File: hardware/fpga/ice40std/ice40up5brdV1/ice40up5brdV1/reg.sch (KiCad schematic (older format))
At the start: 11 parts

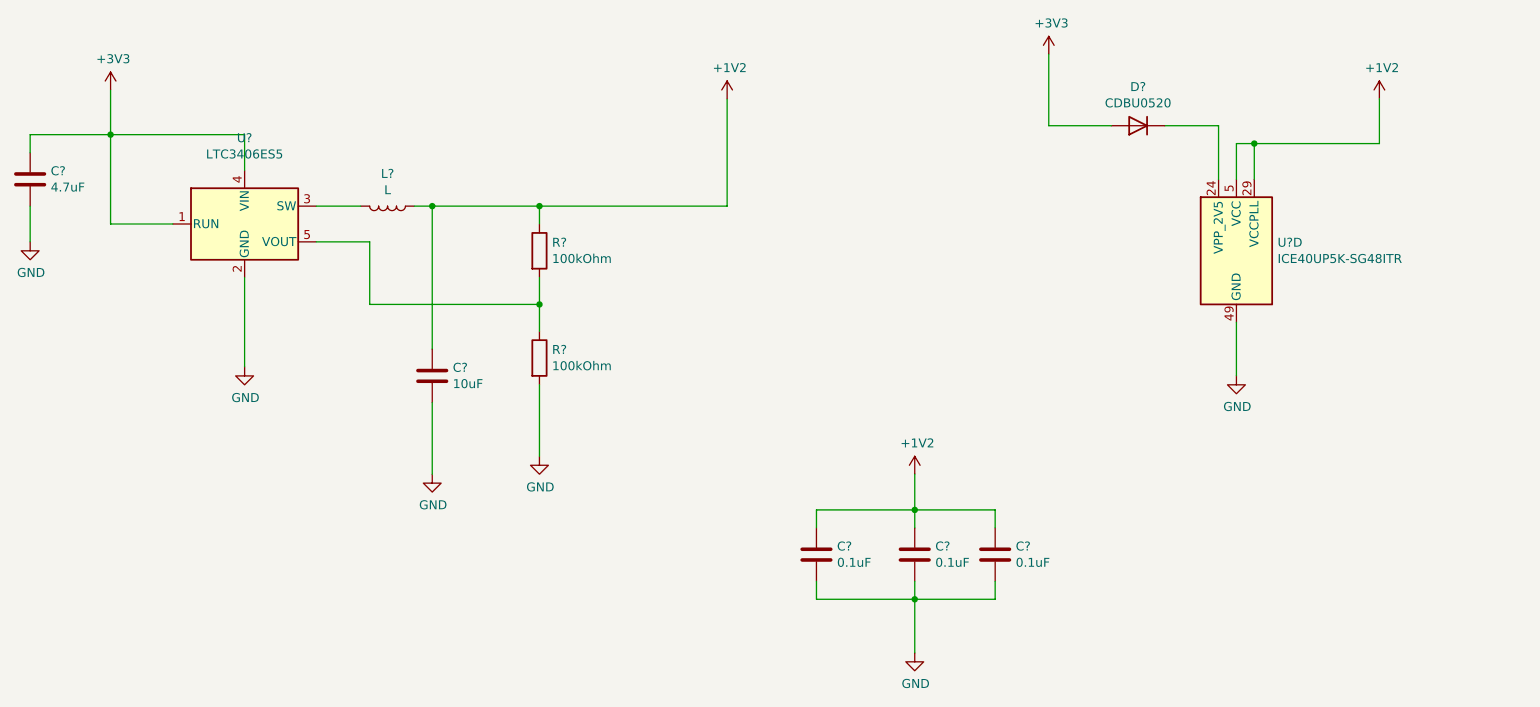
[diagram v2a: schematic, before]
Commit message: usb => mcu => ice40 fpga => NAND flash bridge started
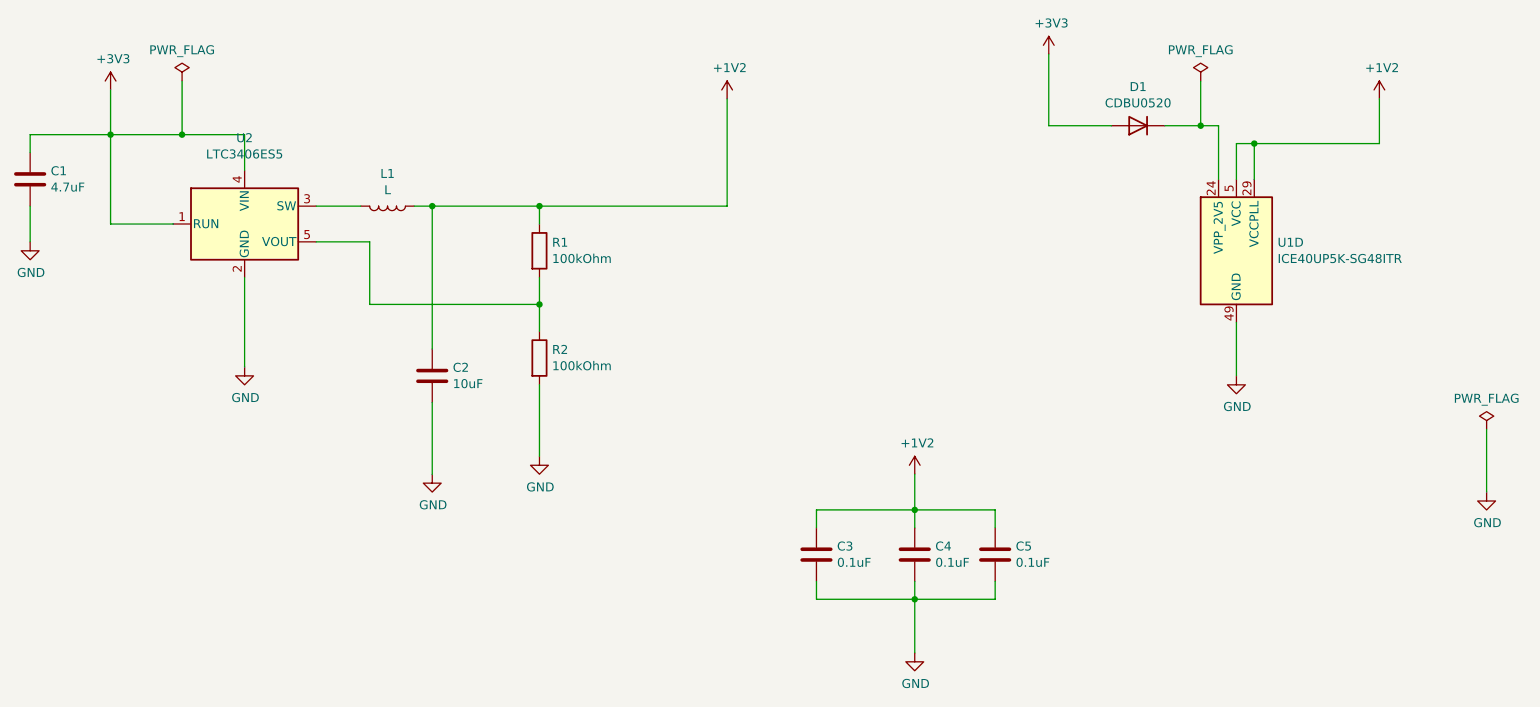
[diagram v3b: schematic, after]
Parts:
- gave numbers to parts that had none: 11
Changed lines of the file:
@@
 $EndDescr
 $Comp
-L FPGA_Lattice:ICE40UP5K-SG48ITR U?
+L FPGA_Lattice:ICE40UP5K-SG48ITR U1
 U 4 1 60A7161F
 P 7850 3250
-F 0 "U?" H 8080 3296 50  0000 L CNN
+F 0 "U1" H 8080 3296 50  0000 L CNN
 F 1 "ICE40UP5K-SG48ITR" H 8080 3205 50  0000 L CNN
 F 2 "Package_DFN_QFN:QFN-48-1EP_7x7mm_P0.5mm_EP5.6x5.6mm" H 7850 1900 50  0001 C CNN
@@
 $EndComp
 $Comp
-L Regulator_Switching:LTC3406ES5 U?
+L Regulator_Switching:LTC3406ES5 U2
 U 1 1 60A7BA3D
 P 2300 3100
-F 0 "U?" H 2300 3581 50  0000 C CNN
+F 0 "U2" H 2300 3581 50  0000 C CNN
 F 1 "LTC3406ES5" H 2300 3490 50  0000 C CNN
 F 2 "Package_TO_SOT_SMD:TSOT-23-5" H 3000 2850 50  0001 C CNN
@@
 $EndComp
 $Comp
-L Device:D D?
+L Device:D D1
 U 1 1 60A801A2
 P 7300 2550
-F 0 "D?" H 7300 2333 50  0000 C CNN
+F 0 "D1" H 7300 2333 50  0000 C CNN
 F 1 "CDBU0520" H 7300 2424 50  0000 C CNN
 F 2 "Diode_SMD:D_0603_1608Metric" H 7300 2550 50  0001 C CNN
@@
 $EndComp
 $Comp
-L Device:L L?
+L Device:L L1
 U 1 1 60A846BB
 P 3100 3000
-F 0 "L?" V 2919 3000 50  0000 C CNN
+F 0 "L1" V 2919 3000 50  0000 C CNN
 F 1 "L" V 3010 3000 50  0000 C CNN
 F 2 "Inductor_SMD:L_1210_3225Metric" H 3100 3000 50  0001 C CNN
@@
 $EndComp
 $Comp
-L Device:R R?
+L Device:R R1
 U 1 1 60A869B1
 P 3950 3250
-F 0 "R?" H 4020 3296 50  0000 L CNN
+F 0 "R1" H 4020 3296 50  0000 L CNN
 F 1 "100kOhm" H 4020 3205 50  0000 L CNN
 F 2 "Resistor_SMD:R_0402_1005Metric" V 3880 3250 50  0001 C CNN
@@
 $EndComp
 $Comp
-L Device:R R?
+L Device:R R2
 U 1 1 60A86DB5
 P 3950 3850
-F 0 "R?" H 4020 3896 50  0000 L CNN
+F 0 "R2" H 4020 3896 50  0000 L CNN
 F 1 "100kOhm" H 4020 3805 50  0000 L CNN
 F 2 "Resistor_SMD:R_0402_1005Metric" V 3880 3850 50  0001 C CNN
@@
 $EndComp
 $Comp
-L power:GND #PWR?
+L power:GND #PWR05
 U 1 1 60A872CB
 P 3950 4400
-F 0 "#PWR?" H 3950 4150 50  0001 C CNN
+F 0 "#PWR05" H 3950 4150 50  0001 C CNN
 F 1 "GND" H 3955 4227 50  0000 C CNN
 F 2 "" H 3950 4400 50  0001 C CNN
@@
 	3950 3550 3950 3400
 $Comp
-L power:GND #PWR?
+L power:GND #PWR03
 U 1 1 60A8868D
 P 2300 3900
-F 0 "#PWR?" H 2300 3650 50  0001 C CNN
+F 0 "#PWR03" H 2300 3650 50  0001 C CNN
 F 1 "GND" H 2305 3727 50  0000 C CNN
 F 2 "" H 2300 3900 50  0001 C CNN
@@
 	2300 3400 2300 3900
 $Comp
-L power:+3V3 #PWR?
+L power:+3V3 #PWR02
 U 1 1 60A899B6
 P 1550 2350
-F 0 "#PWR?" H 1550 2200 50  0001 C CNN
+F 0 "#PWR02" H 1550 2200 50  0001 C CNN
 F 1 "+3V3" H 1565 2523 50  0000 C CNN
 F 2 "" H 1550 2350 50  0001 C CNN
@@
 	2300 2800 2300 2600
 Wire Wire Line
-	2300 2600 1550 2600
+	2300 2600 1950 2600
 Connection ~ 1550 2600
 Wire Wire Line
 	1550 2600 1550 3100
 $Comp
-L Device:C C?
+L Device:C C1
 U 1 1 60A8A29C
 P 1100 2850
-F 0 "C?" H 1215 2896 50  0000 L CNN
+F 0 "C1" H 1215 2896 50  0000 L CNN
 F 1 "4.7uF" H 1215 2805 50  0000 L CNN
 F 2 "Capacitor_SMD:C_0402_1005Metric" H 1138 2700 50  0001 C CNN
@@
 	1100 2600 1550 2600
 $Comp
-L power:GND #PWR?
+L power:GND #PWR01
 U 1 1 60A8AD40
 P 1100 3200
-F 0 "#PWR?" H 1100 2950 50  0001 C CNN
+F 0 "#PWR01" H 1100 2950 50  0001 C CNN
 F 1 "GND" H 1105 3027 50  0000 C CNN
 F 2 "" H 1100 3200 50  0001 C CNN
@@
 	1100 3000 1100 3200
 $Comp
-L Device:C C?
+L Device:C C2
 U 1 1 60A8B955
 P 3350 3950
-F 0 "C?" H 3465 3996 50  0000 L CNN
+F 0 "C2" H 3465 3996 50  0000 L CNN
 F 1 "10uF" H 3465 3905 50  0000 L CNN
 F 2 "Capacitor_SMD:C_0603_1608Metric" H 3388 3800 50  0001 C CNN
@@
 	3350 3000 3950 3000
 $Comp
-L power:GND #PWR?
+L power:GND #PWR04
 U 1 1 60A8CBDB
 P 3350 4500
-F 0 "#PWR?" H 3350 4250 50  0001 C CNN
+F 0 "#PWR04" H 3350 4250 50  0001 C CNN
 F 1 "GND" H 3355 4327 50  0000 C CNN
 F 2 "" H 3350 4500 50  0001 C CNN
@@
 	3350 4100 3350 4500
 $Comp
-L power:+1V2 #PWR?
+L power:+1V2 #PWR06
 U 1 1 60A8DB44
 P 5000 2400
-F 0 "#PWR?" H 5000 2250 50  0001 C CNN
+F 0 "#PWR06" H 5000 2250 50  0001 C CNN
 F 1 "+1V2" H 5015 2573 50  0000 C CNN
 F 2 "" H 5000 2400 50  0001 C CNN
@@
 Connection ~ 3950 3000
 Wire Wire Line
-	7450 2550 7750 2550
+	7450 2550 7650 2550
 Wire Wire Line
 	7750 2550 7750 2850
 $Comp
-L power:+3V3 #PWR?
+L power:+3V3 #PWR09
 U 1 1 60A9198E
 P 6800 2150
-F 0 "#PWR?" H 6800 2000 50  0001 C CNN
+F 0 "#PWR09" H 6800 2000 50  0001 C CNN
 F 1 "+3V3" H 6815 2323 50  0000 C CNN
 F 2 "" H 6800 2150 50  0001 C CNN
@@
 	6800 2550 7150 2550
 $Comp
-L power:+1V2 #PWR?
+L power:+1V2 #PWR011
 U 1 1 60A94F17
 P 8650 2400
-F 0 "#PWR?" H 8650 2250 50  0001 C CNN
+F 0 "#PWR011" H 8650 2250 50  0001 C CNN
 F 1 "+1V2" H 8665 2573 50  0000 C CNN
 F 2 "" H 8650 2400 50  0001 C CNN
@@
 	7950 2850 7950 2650
 Connection ~ 7950 2650
-Wire Wire Line
-	7950 2650 8650 2650
-$Comp
-L power:+1V2 #PWR?
+$Comp
+L power:+1V2 #PWR07
 U 1 1 60A96F10
 P 6050 4500
-F 0 "#PWR?" H 6050 4350 50  0001 C CNN
+F 0 "#PWR07" H 6050 4350 50  0001 C CNN
 F 1 "+1V2" H 6065 4673 50  0000 C CNN
 F 2 "" H 6050 4500 50  0001 C CNN
@@
 $EndComp
 $Comp
-L Device:C C?
+L Device:C C3
 U 1 1 60A9752A
 P 5500 4950
-F 0 "C?" H 5615 4996 50  0000 L CNN
+F 0 "C3" H 5615 4996 50  0000 L CNN
 F 1 "0.1uF" H 5615 4905 50  0000 L CNN
 F 2 "Capacitor_SMD:C_0402_1005Metric" H 5538 4800 50  0001 C CNN
@@
 $EndComp
 $Comp
-L Device:C C?
+L Device:C C5
 U 1 1 60A97958
 P 6500 4950
-F 0 "C?" H 6615 4996 50  0000 L CNN
+F 0 "C5" H 6615 4996 50  0000 L CNN
 F 1 "0.1uF" H 6615 4905 50  0000 L CNN
 F 2 "Capacitor_SMD:C_0402_1005Metric" H 6538 4800 50  0001 C CNN
@@
 	6500 5200 6500 5100
 $Comp
-L power:GND #PWR?
+L power:GND #PWR010
 U 1 1 60A9A1A4
 P 7850 3950
-F 0 "#PWR?" H 7850 3700 50  0001 C CNN
+F 0 "#PWR010" H 7850 3700 50  0001 C CNN
 F 1 "GND" H 7855 3777 50  0000 C CNN
 F 2 "" H 7850 3950 50  0001 C CNN
@@
 $EndComp
 $Comp
-L power:GND #PWR?
+L power:GND #PWR08
 U 1 1 60A9A678
 P 6050 5500
-F 0 "#PWR?" H 6050 5250 50  0001 C CNN
+F 0 "#PWR08" H 6050 5250 50  0001 C CNN
 F 1 "GND" H 6055 5327 50  0000 C CNN
 F 2 "" H 6050 5500 50  0001 C CNN
@@
 	7850 3650 7850 3950
 $Comp
-L Device:C C?
+L Device:C C4
 U 1 1 60A9DB64
 P 6050 4950
-F 0 "C?" H 6165 4996 50  0000 L CNN
+F 0 "C4" H 6165 4996 50  0000 L CNN
 F 1 "0.1uF" H 6165 4905 50  0000 L CNN
 F 2 "Capacitor_SMD:C_0402_1005Metric" H 6088 4800 50  0001 C CNN
@@
 Wire Wire Line
 	6050 4800 6050 4700
+$Comp
+L power:PWR_FLAG #FLG0101
+U 1 1 60B35337
+P 7650 2300
+F 0 "#FLG0101" H 7650 2375 50  0001 C CNN
+F 1 "PWR_FLAG" H 7650 2473 50  0000 C CNN
+F 2 "" H 7650 2300 50  0001 C CNN
+F 3 "~" H 7650 2300 50  0001 C CNN
+	1    7650 2300
+	1    0    0    -1
+$EndComp
+Wire Wire Line
+	7650 2300 7650 2550
+Connection ~ 7650 2550
+Wire Wire Line
+	7650 2550 7750 2550
+$Comp
+L power:PWR_FLAG #FLG0103
+U 1 1 60B373B2
+P 1950 2300
+F 0 "#FLG0103" H 1950 2375 50  0001 C CNN
+F 1 "PWR_FLAG" H 1950 2473 50  0000 C CNN
+F 2 "" H 1950 2300 50  0001 C CNN
+F 3 "~" H 1950 2300 50  0001 C CNN
+	1    1950 2300
+	1    0    0    -1
+$EndComp
+$Comp
+L power:PWR_FLAG #FLG0104
+U 1 1 60B37B07
+P 9250 4250
+F 0 "#FLG0104" H 9250 4325 50  0001 C CNN
+F 1 "PWR_FLAG" H 9250 4423 50  0000 C CNN
+F 2 "" H 9250 4250 50  0001 C CNN
+F 3 "~" H 9250 4250 50  0001 C CNN
+	1    9250 4250
+	1    0    0    -1
+$EndComp
+$Comp
+L power:GND #PWR0103
+U 1 1 60B3812C
+P 9250 4600
+F 0 "#PWR0103" H 9250 4350 50  0001 C CNN
+F 1 "GND" H 9255 4427 50  0000 C CNN
+F 2 "" H 9250 4600 50  0001 C CNN
+F 3 "" H 9250 4600 50  0001 C CNN
+	1    9250 4600
+	1    0    0    -1
+$EndComp
+Wire Wire Line
+	9250 4250 9250 4600
+Wire Wire Line
+	1950 2300 1950 2600
+Connection ~ 1950 2600
+Wire Wire Line
+	1950 2600 1550 2600
+Wire Wire Line
+	7950 2650 8650 2650
 $EndSCHEMATC

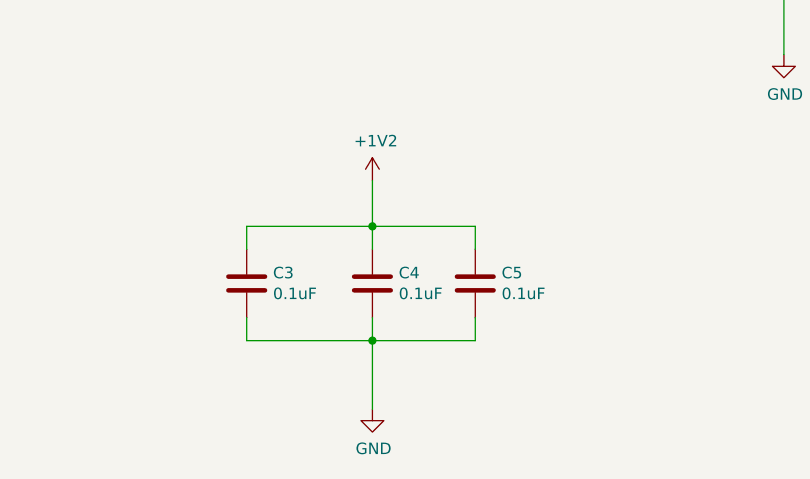
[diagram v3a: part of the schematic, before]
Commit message: usb => mcu => ice40 fpga => NAND flash bridge started
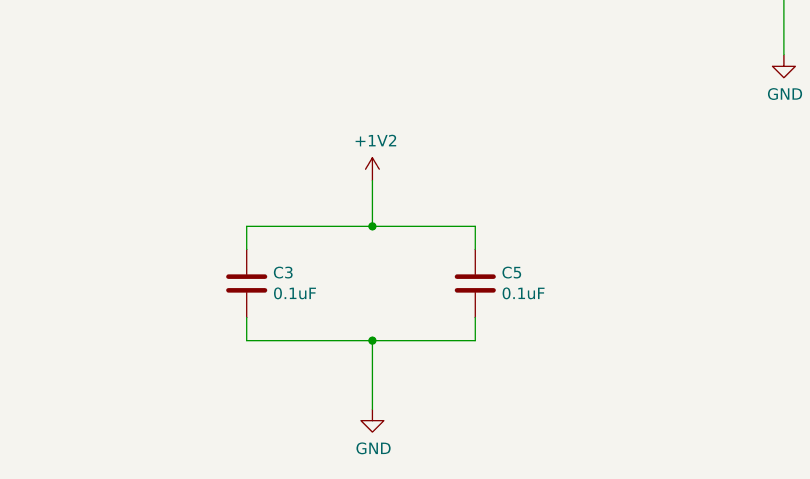
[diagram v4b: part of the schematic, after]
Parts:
- removed C4: 0.1uF, Capacitor_SMD:C_0402_1005Metric, symbol Device:C
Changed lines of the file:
@@
-	1    0    0    -1
-$EndComp
-$Comp
-L Device:C C5
-U 1 1 60A97958
-P 6500 4950
-F 0 "C5" H 6615 4996 50  0000 L CNN
-F 1 "0.1uF" H 6615 4905 50  0000 L CNN
-F 2 "Capacitor_SMD:C_0402_1005Metric" H 6538 4800 50  0001 C CNN
-F 3 "~" H 6500 4950 50  0001 C CNN
-	1    6500 4950
 	1    0    0    -1
 $EndComp
@@
 	5500 4700 6050 4700
 Wire Wire Line
-	6500 4700 6500 4800
-Wire Wire Line
 	6050 4500 6050 4700
 Wire Wire Line
@@
 Wire Wire Line
 	5500 5200 6050 5200
-Wire Wire Line
-	6500 5200 6500 5100
 $Comp
 L power:GND #PWR010
@@
 Connection ~ 6050 5200
 Wire Wire Line
-	6050 5200 6500 5200
-Wire Wire Line
 	7850 3650 7850 3950
-$Comp
-L Device:C C4
-U 1 1 60A9DB64
-P 6050 4950
-F 0 "C4" H 6165 4996 50  0000 L CNN
-F 1 "0.1uF" H 6165 4905 50  0000 L CNN
-F 2 "Capacitor_SMD:C_0402_1005Metric" H 6088 4800 50  0001 C CNN
-F 3 "~" H 6050 4950 50  0001 C CNN
-	1    6050 4950
-	1    0    0    -1
-$EndComp
 Connection ~ 6050 4700
-Wire Wire Line
-	6050 4700 6500 4700
-Wire Wire Line
-	6050 5200 6050 5100
-Wire Wire Line
-	6050 4800 6050 4700
 $Comp
 L power:PWR_FLAG #FLG0101
@@
 Wire Wire Line
 	7950 2650 8650 2650
+Wire Wire Line
+	6050 4700 6500 4700
+Wire Wire Line
+	6050 5200 6500 5200
+Wire Wire Line
+	6500 5200 6500 5100
+Wire Wire Line
+	6500 4700 6500 4800
+$Comp
+L Device:C C5
+U 1 1 60A97958
+P 6500 4950
+F 0 "C5" H 6615 4996 50  0000 L CNN
+F 1 "0.1uF" H 6615 4905 50  0000 L CNN
+F 2 "Capacitor_SMD:C_0402_1005Metric" H 6538 4800 50  0001 C CNN
+F 3 "~" H 6500 4950 50  0001 C CNN
+	1    6500 4950
+	1    0    0    -1
+$EndComp
 $EndSCHEMATC
